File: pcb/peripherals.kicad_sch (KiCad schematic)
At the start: 42 parts, among them J4 Conn_01x03, J5 Conn_01x03, J6 Conn_01x03, J7 Conn_01x03, Q7 BSS138, Q8 AO3407A, SW10 GENERAL, SW4 SW_DIP_x04, SW7 GENERAL, SW8 GENERAL, SW9 GENERAL, U14 PCF8563T, U15 PCA9555PW, U16 CAT24C32YI-GT3, Y2 32.768kHz 9pF

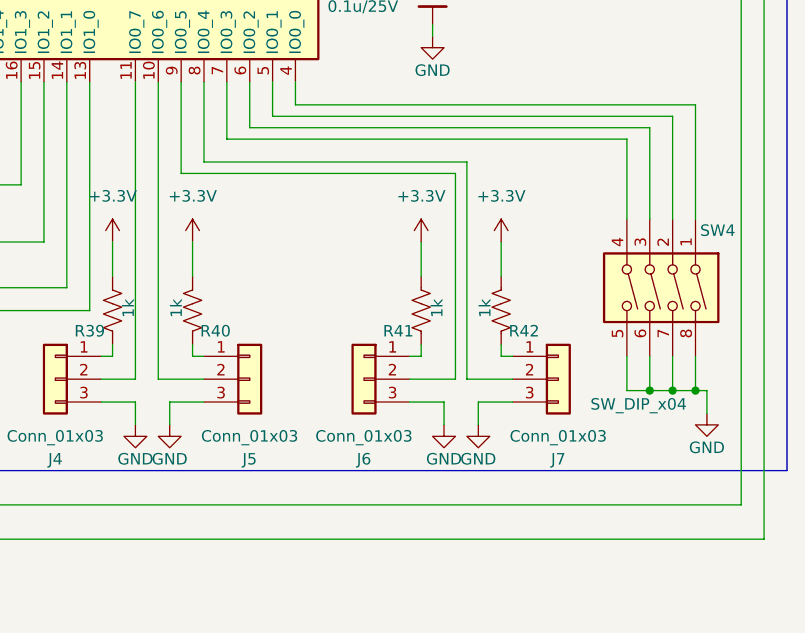
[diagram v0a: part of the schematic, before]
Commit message: Add SA818S-V sheet, update GPS antenna connector, MCU GPIO reassignments
- New SA818S-V sheet (U19): UART/PTT/MIC_IN wired; VBAT, ANT, PD, H/L
  still open (see sa818_pinout.md).
- gps.kicad_sch: J10 swapped to Amphenol 132289 edge-launch SMD SMA
  (same part planned for the SA818 antenna connector).
- mcu-esp32.kicad_sch: SA818 UART on IO6/IO7, PTT on IO16 (direct FET
  drive via Q10, not the originally-planned AND-gate scheme).
- peripherals.kicad_sch: in-progress PCA9555 channel changes.

Co-Authored-By: Claude Sonnet 5 <noreply@anthropic.com>
Claude-Session: https://claude.ai/code/session_01LhLkuH6sQ5GbUZ61bG7p2h
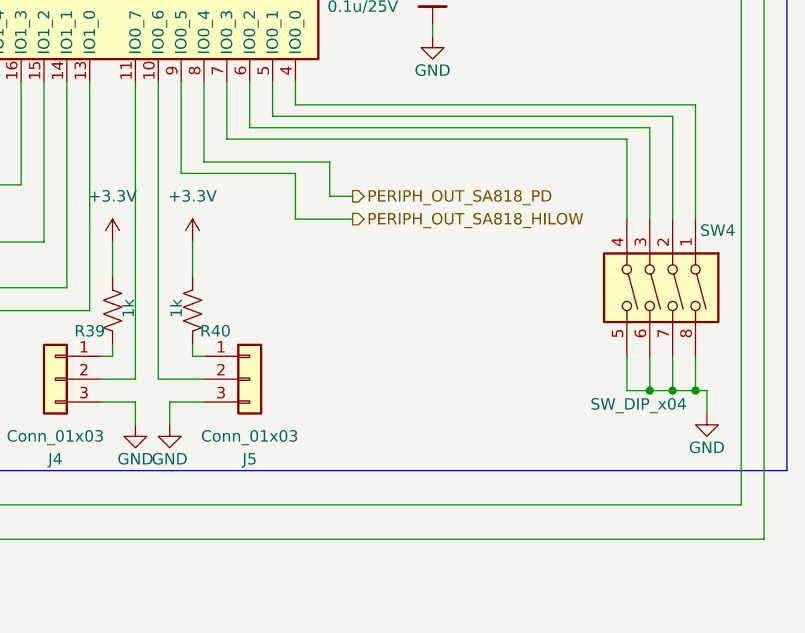
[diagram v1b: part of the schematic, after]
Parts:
- removed J6, J7: Conn_01x03, Connector_JST:JST_PH_B3B-PH-SM4-TB_1x03-1MP_P2.00mm_Vertical, symbol Connector_Generic:Conn_01x03
- removed R41, R42: 1k, Resistor_SMD:R_0603_1608Metric, symbol Device:R_US
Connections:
- net PERIPH_OUT_SA818_HILOW: now reaches U15.9 (IO0_5)
- net PERIPH_OUT_SA818_PD: now reaches U15.8 (IO0_4)

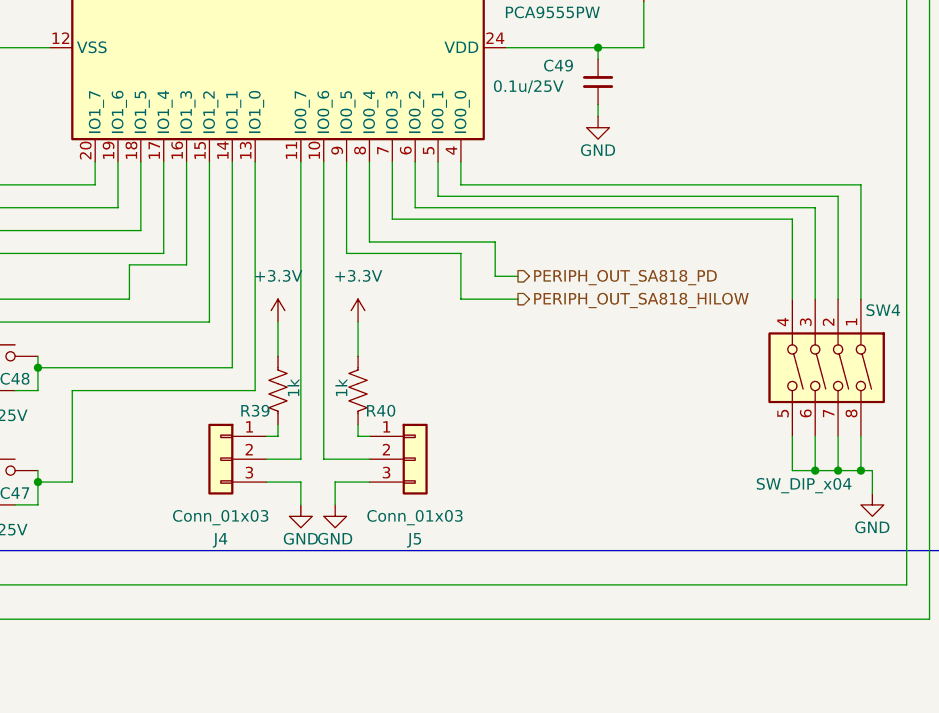
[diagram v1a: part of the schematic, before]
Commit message: Wire SA818 PD/H-L and PTT opto, GPS power gating with bench bypass, RF detector groundwork
- SA818S-V: wire PD/H-L to PCA9555 expander outputs; swap PTT-keying FET
  for PC817 optocoupler isolation on the shared SA818S/external-HT PTT line
- GPS: add Q10 (AO3407A) high-side P-FET gating VCC+VCC_IO together for
  genuine hardware backup mode, driven via Q13 level-shifter from a new
  PCA9555 output (PERIPH_OUT_GPS_PWRON); add JP28 as a source-to-drain
  bench bypass across Q10 for unconditional power during bring-up; wire
  EXTINT to another PCA9555 output (PERIPH_OUT_GPS_EXTINT, pulled low by
  R57) to experiment with UART software-standby + external wake
- peripherals: reassign PCA9555 channels for the above plus SA818 PD/H-L
- audio/mcu-esp32: forward-power detector tap wiring groundwork
- docs: add vhf_matching_detector.md (matching network + RF detector BOM
  and layout), index it in _docs/README.md

Co-Authored-By: Claude Sonnet 5 <noreply@anthropic.com>
Claude-Session: https://claude.ai/code/session_01LhLkuH6sQ5GbUZ61bG7p2h
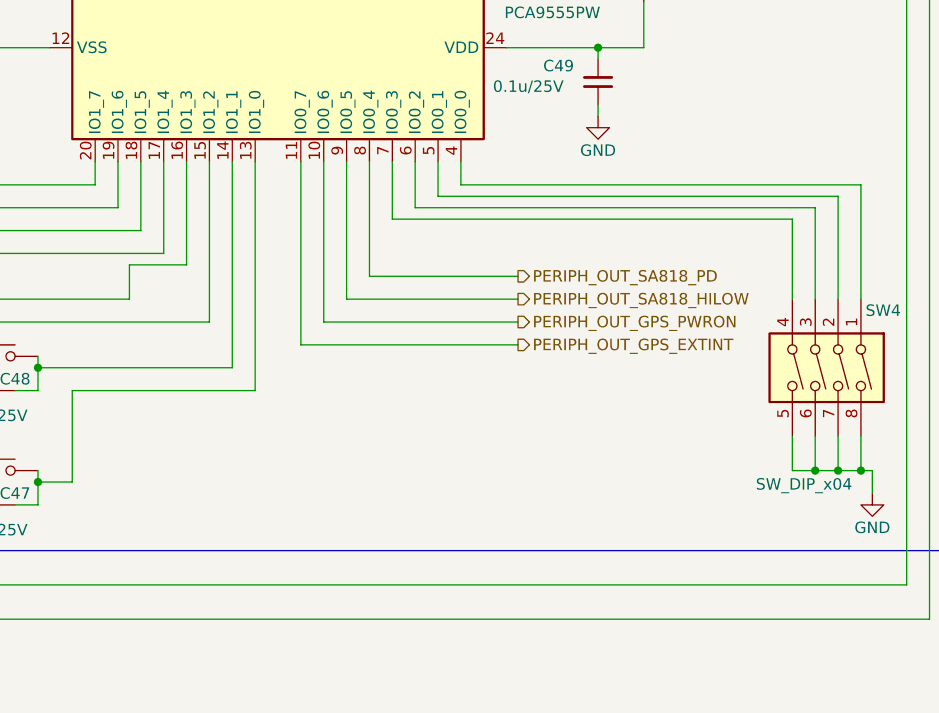
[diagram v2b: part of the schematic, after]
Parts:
- removed J4, J5: Conn_01x03, Connector_JST:JST_PH_B3B-PH-SM4-TB_1x03-1MP_P2.00mm_Vertical, symbol Connector_Generic:Conn_01x03
- removed R39, R40: 1k, Resistor_SMD:R_0603_1608Metric, symbol Device:R_US
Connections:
- net PERIPH_OUT_GPS_PWRON: now reaches U15.10 (IO0_6)
- net PERIPH_OUT_GPS_EXTINT: now reaches U15.11 (IO0_7)
